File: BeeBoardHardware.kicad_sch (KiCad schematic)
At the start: 46 parts, among them J2 USB_C_Receptacle_USB2.0_16P, J3 Conn_01x02, J4 Conn_01x11, Q1 AO3413, SW2 SW_Push, U1 MCP16311x-xMNY, U2 BQ24074RGT, U3 USBLC6-2SC6, U4 LC709203FQH-01TWG, U5 STM6600DQ25DM6F

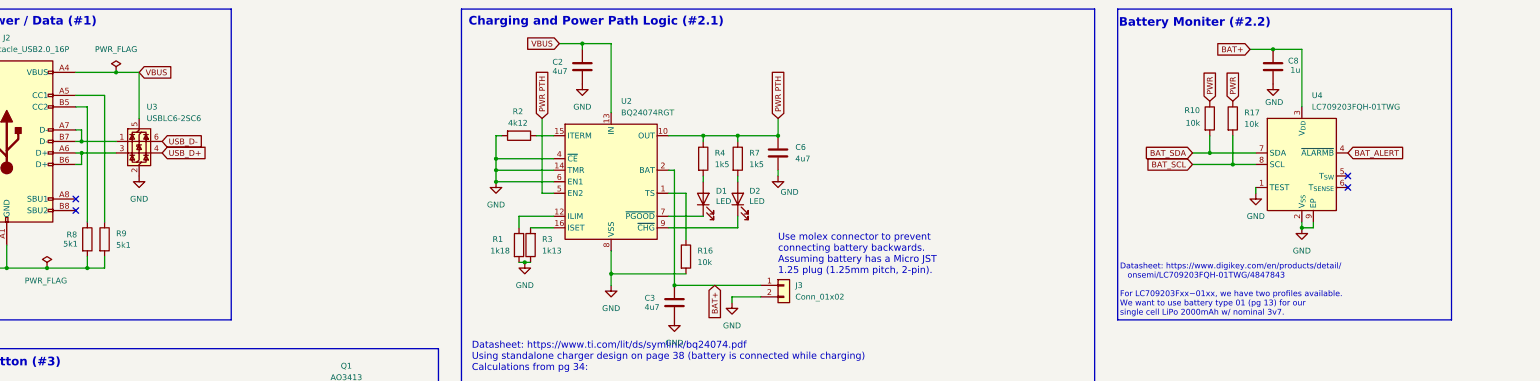
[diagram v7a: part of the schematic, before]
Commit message: routed more traces
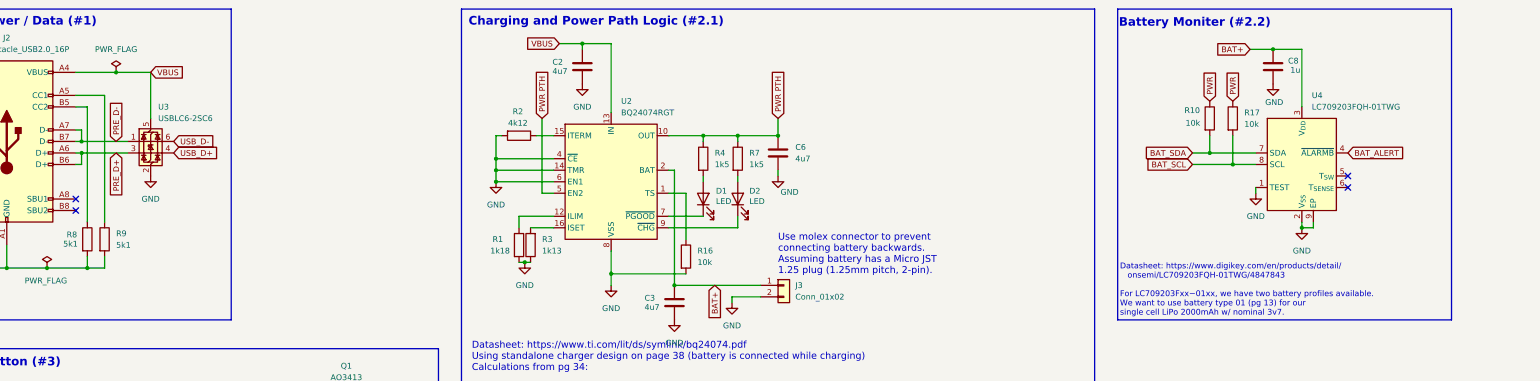
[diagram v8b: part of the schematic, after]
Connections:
- net PRE_D+: now reaches J2.A6 (D+), J2.B6 (D+), U3.3 (I/O2)
- net PRE_D-: now reaches J2.A7 (D-), J2.B7 (D-), U3.1 (I/O1)
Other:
- note added: "Datasheet: https://www.digikey.com/en/products/detail/ onsemi/LC709203FQH-01TWG/4847843 For LC709203Fxx−01xx, we have two battery profiles available. We want to use battery type 01 (pg 13) for our single cell LiPo 2000mAh w/ nominal 3v7."
- note removed: "Datasheet: https://www.digikey.com/en/products/detail/ onsemi/LC709203FQH-01TWG/4847843 For LC709203Fxx−01xx, we have two profiles available. We want to use battery type 01 (pg 13) for our single cell LiPo 2000mAh w/ nominal 3v7."
- company: LMakers -> (none)
- moved on the sheet: U3
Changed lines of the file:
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@@
 		(date "2025-02-09")
 		(rev "V1")
-		(company "LMakers")
 	)
 	(junction
@@
 	(wire
 		(pts
-			(xy 54.61 48.26) (xy 62.23 48.26)
+			(xy 54.61 48.26) (xy 64.77 48.26)
 		)
 		(stroke
@@
 	(wire
 		(pts
-			(xy 67.31 33.02) (xy 67.31 43.18)
+			(xy 69.85 33.02) (xy 69.85 43.18)
 		)
 		(stroke
@@
 	(wire
 		(pts
-			(xy 62.23 33.02) (xy 67.31 33.02)
+			(xy 62.23 33.02) (xy 69.85 33.02)
 		)
 		(stroke
@@
 	(wire
 		(pts
-			(xy 54.61 50.8) (xy 62.23 50.8)
+			(xy 54.61 50.8) (xy 64.77 50.8)
 		)
 		(stroke
@@
 		)
 	)
-	(text "Datasheet: https://www.digikey.com/en/products/detail/\n   onsemi/LC709203FQH-01TWG/4847843\n\nFor LC709203Fxx−01xx, we have two profiles available. \nWe want to use battery type 01 (pg 13) for our \nsingle cell LiPo 2000mAh w/ nominal 3v7."
+	(text "Datasheet: https://www.digikey.com/en/products/detail/\n   onsemi/LC709203FQH-01TWG/4847843\n\nFor LC709203Fxx−01xx, we have two battery profiles available. \nWe want to use battery type 01 (pg 13) for our \nsingle cell LiPo 2000mAh w/ nominal 3v7."
 		(exclude_from_sim no)
 		(at 283.718 81.026 0)
@@
 		)
 	)
+	(global_label "PRE_D-"
+		(shape input)
+		(at 62.23 48.26 90)
+		(fields_autoplaced yes)
+		(effects
+			(font
+				(size 1.27 1.27)
+			)
+			(justify left)
+		)
+		(property "Intersheetrefs" "${INTERSHEET_REFS}"
+			(at 62.23 37.7758 90)
+			(effects
+				(font
+					(size 1.27 1.27)
+				)
+				(justify left)
+				(hide yes)
+			)
+		)
+	)
 	(global_label "VBUS"
 		(shape input)
-		(at 67.31 33.02 0)
+		(at 69.85 33.02 0)
 		(fields_autoplaced yes)
 		(effects
@@
 		)
 		(property "Intersheetrefs" "${INTERSHEET_REFS}"
-			(at 75.1938 33.02 0)
+			(at 77.7338 33.02 0)
 			(effects
 				(font
@@
 		)
 	)
+	(global_label "PRE_D+"
+		(shape input)
+		(at 62.23 50.8 270)
+		(fields_autoplaced yes)
+		(effects
+			(font
+				(size 1.27 1.27)
+			)
+			(justify right)
+		)
+		(property "Intersheetrefs" "${INTERSHEET_REFS}"
+			(at 62.23 61.2842 90)
+			(effects
+				(font
+					(size 1.27 1.27)
+				)
+				(justify right)
+				(hide yes)
+			)
+		)
+	)
 	(global_label "+3v3"
 		(shape input)
@@
 	(global_label "USB_D+"
 		(shape input)
-		(at 72.39 50.8 0)
+		(at 74.93 50.8 0)
 		(fields_autoplaced yes)
 		(effects
@@
 		)
 		(property "Intersheetrefs" "${INTERSHEET_REFS}"
-			(at 82.9952 50.8 0)
+			(at 85.5352 50.8 0)
 			(effects
 				(font
@@
 	(global_label "USB_D-"
 		(shape input)
-		(at 72.39 48.26 0)
+		(at 74.93 48.26 0)
 		(fields_autoplaced yes)
 		(effects
@@
 		)
 		(property "Intersheetrefs" "${INTERSHEET_REFS}"
-			(at 82.9952 48.26 0)
+			(at 85.5352 48.26 0)
 			(effects
 				(font
@@
 	(symbol
 		(lib_id "power:GND")
-		(at 67.31 55.88 0)
+		(at 69.85 55.88 0)
 		(unit 1)
 		(exclude_from_sim no)
@@
 		(fields_autoplaced yes)
 		(property "Reference" "#PWR013"
-			(at 67.31 62.23 0)
+			(at 69.85 62.23 0)
 			(effects
 				(font
@@
 		)
 		(property "Value" "GND"
-			(at 67.31 60.96 0)
+			(at 69.85 60.96 0)
 			(effects
 				(font
@@
 		)
 		(property "Footprint" ""
-			(at 67.31 55.88 0)
+			(at 69.85 55.88 0)
 			(effects
 				(font
@@
 		)
 		(property "Datasheet" ""
-			(at 67.31 55.88 0)
+			(at 69.85 55.88 0)
 			(effects
 				(font
@@
 		)
 		(property "Description" "Power symbol creates a global label with name \"GND\" , ground"
-			(at 67.31 55.88 0)
+			(at 69.85 55.88 0)
 			(effects
 				(font
@@
 	(symbol
 		(lib_id "Power_Protection:USBLC6-2SC6")
-		(at 67.31 48.26 0)
+		(at 69.85 48.26 0)
 		(unit 1)
 		(exclude_from_sim no)
@@
 		(fields_autoplaced yes)
 		(property "Reference" "U3"
-			(at 68.9611 40.64 0)
+			(at 71.5011 40.64 0)
 			(effects
 				(font
@@
 		)
 		(property "Value" "USBLC6-2SC6"
-			(at 68.9611 43.18 0)
+			(at 71.5011 43.18 0)
 			(effects
 				(font
@@
 		)
 		(property "Footprint" "Package_TO_SOT_SMD:SOT-23-6"
-			(at 68.58 54.61 0)
+			(at 71.12 54.61 0)
 			(effects
 				(font
@@
 		)
 		(property "Datasheet" "https://www.st.com/resource/en/datasheet/usblc6-2.pdf"
-			(at 68.58 56.515 0)
+			(at 71.12 56.515 0)
 			(effects
 				(font
@@
 		)
 		(property "Description" "Very low capacitance ESD protection diode, 2 data-line, SOT-23-6"
-			(at 67.31 48.26 0)
+			(at 69.85 48.26 0)
 			(effects
 				(font
@@
 		)
 		(property "Digikey Link" ""
-			(at 67.31 48.26 0)
+			(at 69.85 48.26 0)
 			(effects
 				(font
@@
 		)
 		(property "Manufacturer Product Number" ""
-			(at 67.31 48.26 0)
+			(at 69.85 48.26 0)
 			(effects
 				(font
